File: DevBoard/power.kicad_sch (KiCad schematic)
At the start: 31 parts, among them U201 INA190A5IDDFR, U202 INA190A1IDDFR, U203 HT7550-1, U204 TPS62177DQCR

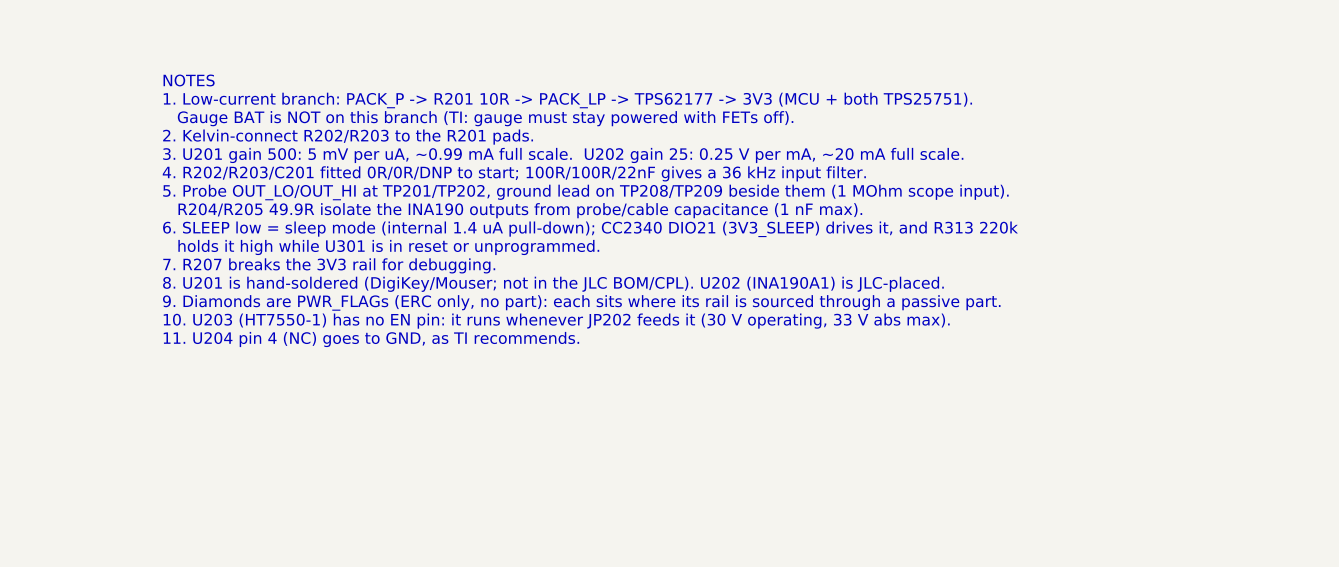
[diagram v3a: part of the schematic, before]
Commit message: Dev board: cut JLC extended parts 37 -> 27 for a 2-board build
tools/bom_fee_cut.py (one-shot); README item 44. At 2 boards the costed
BOM goes from $124.28 to $108.49 per board.
- Basic/preferred swaps, no footprint changes: C313 -> C1548, C315/C314
  -> C1550, C401/C402 -> C1530 (X7R), R433/R434 -> 120k/22k 1 %
  (PP5V 5.16 V), C443/C543 -> 100 uF 35 V Honor polymer (same as C421).
- Hand-fit from LCSC: BT101-BT104, the 13 Harwin test loops, U202, D105
  (dev-only; out of the position file).
- Board: fields refreshed by netlist_to_board.py; also includes Logan's
  block move made in KiCad. DRC parity 0; ERC unchanged.

Co-Authored-By: Claude Opus 5.5 <noreply@anthropic.com>
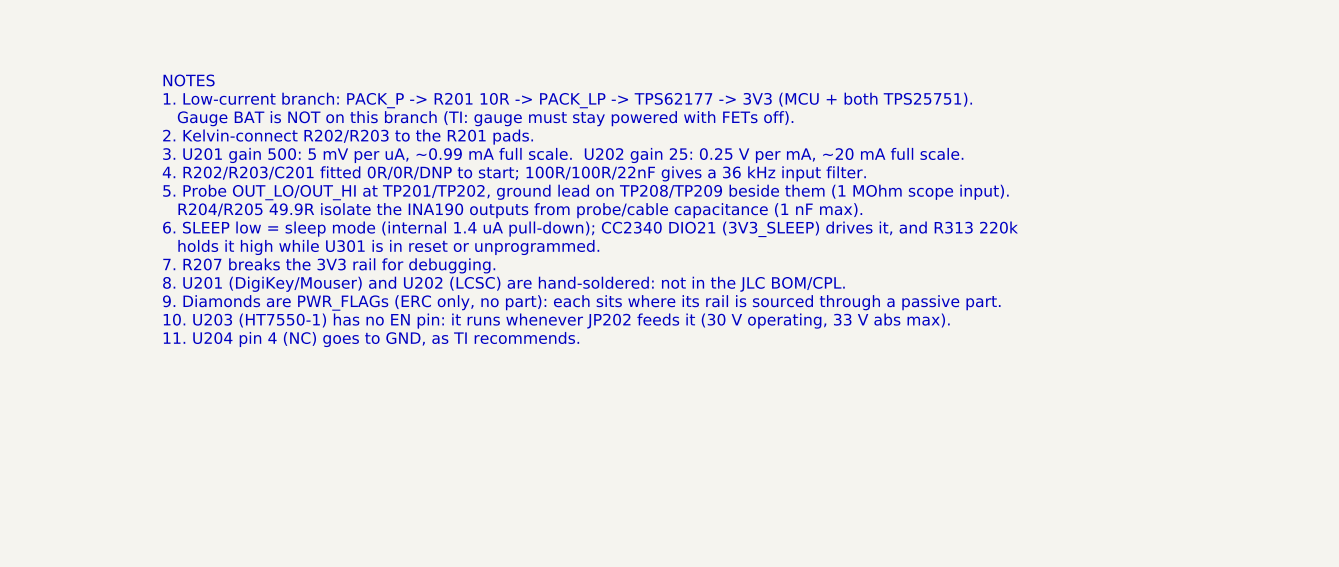
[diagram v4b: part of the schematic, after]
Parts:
- TP201, TP202, TP203, TP208, TP209: LCSC C55121754 -> (none); Sourcing (none) -> Hand-solder, not JLC assembled (test loop, dev only; saves 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
- U202: LCSC C1852068 -> (none); Sourcing JLC assembled (LCSC C1852068, 1,700 in stock 2026-10-13) -> Hand-solder, not JLC assembled (dev-only sleep-current ampl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
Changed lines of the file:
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@@
 		)
 	)
-	(text "NOTES\n1. Low-current branch: PACK_P -> R201 10R -> PACK_LP -> TPS62177 -> 3V3 (MCU + both TPS25751).\n   Gauge BAT is NOT on this branch (TI: gauge must stay powered with FETs off).\n2. Kelvin-connect R202/R203 to the R201 pads.\n3. U201 gain 500: 5 mV per uA, ~0.99 mA full scale.  U202 gain 25: 0.25 V per mA, ~20 mA full scale.\n4. R202/R203/C201 fitted 0R/0R/DNP to start; 100R/100R/22nF gives a 36 kHz input filter.\n5. Probe OUT_LO/OUT_HI at TP201/TP202, ground lead on TP208/TP209 beside them (1 MOhm scope input).\n   R204/R205 49.9R isolate the INA190 outputs from probe/cable capacitance (1 nF max).\n6. SLEEP low = sleep mode (internal 1.4 uA pull-down); CC2340 DIO21 (3V3_SLEEP) drives it, and R313 220k\n   holds it high while U301 is in reset or unprogrammed.\n7. R207 breaks the 3V3 rail for debugging.\n8. U201 is hand-soldered (DigiKey/Mouser; not in the JLC BOM/CPL). U202 (INA190A1) is JLC-placed.\n9. Diamonds are PWR_FLAGs (ERC only, no part): each sits where its rail is sourced through a passive part.\n10. U203 (HT7550-1) has no EN pin: it runs whenever JP202 feeds it (30 V operating, 33 V abs max).\n11. U204 pin 4 (NC) goes to GND, as TI recommends."
+	(text "NOTES\n1. Low-current branch: PACK_P -> R201 10R -> PACK_LP -> TPS62177 -> 3V3 (MCU + both TPS25751).\n   Gauge BAT is NOT on this branch (TI: gauge must stay powered with FETs off).\n2. Kelvin-connect R202/R203 to the R201 pads.\n3. U201 gain 500: 5 mV per uA, ~0.99 mA full scale.  U202 gain 25: 0.25 V per mA, ~20 mA full scale.\n4. R202/R203/C201 fitted 0R/0R/DNP to start; 100R/100R/22nF gives a 36 kHz input filter.\n5. Probe OUT_LO/OUT_HI at TP201/TP202, ground lead on TP208/TP209 beside them (1 MOhm scope input).\n   R204/R205 49.9R isolate the INA190 outputs from probe/cable capacitance (1 nF max).\n6. SLEEP low = sleep mode (internal 1.4 uA pull-down); CC2340 DIO21 (3V3_SLEEP) drives it, and R313 220k\n   holds it high while U301 is in reset or unprogrammed.\n7. R207 breaks the 3V3 rail for debugging.\n8. U201 (DigiKey/Mouser) and U202 (LCSC) are hand-soldered: not in the JLC BOM/CPL.\n9. Diamonds are PWR_FLAGs (ERC only, no part): each sits where its rail is sourced through a passive part.\n10. U203 (HT7550-1) has no EN pin: it runs whenever JP202 feeds it (30 V operating, 33 V abs max).\n11. U204 pin 4 (NC) goes to GND, as TI recommends."
 		(exclude_from_sim no)
 		(at 215.9 129.54 0)
@@
 		(in_bom yes)
 		(on_board yes)
-		(in_pos_files yes)
+		(in_pos_files no)
 		(dnp no)
 		(property "Reference" "TP203"
@@
 			)
 		)
-		(property "LCSC" "C55121754"
+		(property "LCSC" ""
 			(at 190.5 165.1 0)
 			(hide yes)
@@
 			)
 		)
+		(property "Sourcing" "Hand-solder, not JLC assembled (test loop, dev only; saves a JLC extended-part fee; LCSC C55121754 RH-S2761-46R (ronghe; Harwin S2761-46R equivalent))"
+			(at 190.5 165.1 0)
+			(hide yes)
+			(show_name no)
+			(do_not_autoplace no)
+			(effects
+				(font
+					(size 1.27 1.27)
+				)
+			)
+		)
 		(pin "1"
 		)
@@
 		(in_bom yes)
 		(on_board yes)
-		(in_pos_files yes)
+		(in_pos_files no)
 		(dnp no)
 		(property "Reference" "TP201"
@@
 			)
 		)
-		(property "LCSC" "C55121754"
+		(property "LCSC" ""
 			(at 152.4 144.78 0)
 			(hide yes)
@@
 			)
 		)
+		(property "Sourcing" "Hand-solder, not JLC assembled (test loop, dev only; saves a JLC extended-part fee; LCSC C55121754 RH-S2761-46R (ronghe; Harwin S2761-46R equivalent))"
+			(at 152.4 144.78 0)
+			(hide yes)
+			(show_name no)
+			(do_not_autoplace no)
+			(effects
+				(font
+					(size 1.27 1.27)
+				)
+			)
+		)
 		(pin "1"
 		)
@@
 		(in_bom yes)
 		(on_board yes)
-		(in_pos_files yes)
+		(in_pos_files no)
 		(dnp no)
 		(property "Reference" "TP208"
@@
 			)
 		)
-		(property "LCSC" "C55121754"
+		(property "LCSC" ""
 			(at 172.72 152.4 0)
 			(hide yes)
@@
 			)
 		)
+		(property "Sourcing" "Hand-solder, not JLC assembled (test loop, dev only; saves a JLC extended-part fee; LCSC C55121754 RH-S2761-46R (ronghe; Harwin S2761-46R equivalent))"
+			(at 172.72 152.4 0)
+			(hide yes)
+			(show_name no)
+			(do_not_autoplace no)
+			(effects
+				(font
+					(size 1.27 1.27)
+				)
+			)
+		)
 		(pin "1"
 		)
@@
 		(in_bom yes)
 		(on_board yes)
-		(in_pos_files yes)
+		(in_pos_files no)
 		(dnp no)
 		(property "Reference" "TP209"
@@
 			)
 		)
-		(property "LCSC" "C55121754"
+		(property "LCSC" ""
 			(at 172.72 190.5 0)
 			(hide yes)
@@
 			)
 		)
+		(property "Sourcing" "Hand-solder, not JLC assembled (test loop, dev only; saves a JLC extended-part fee; LCSC C55121754 RH-S2761-46R (ronghe; Harwin S2761-46R equivalent))"
+			(at 172.72 190.5 0)
+			(hide yes)
+			(show_name no)
+			(do_not_autoplace no)
+			(effects
+				(font
+					(size 1.27 1.27)
+				)
+			)
+		)
 		(pin "1"
 		)
@@
 		(in_bom yes)
 		(on_board yes)
-		(in_pos_files yes)
+		(in_pos_files no)
 		(dnp no)
 		(property "Reference" "U202"
@@
 			)
 		)
-		(property "LCSC" "C1852068"
+		(property "LCSC" ""
 			(at 109.22 182.88 0)
 			(hide yes)
@@
 			)
 		)
-		(property "Sourcing" "JLC assembled (LCSC C1852068, 1,700 in stock 2026-10-13)"
+		(property "Sourcing" "Hand-solder, not JLC assembled (dev-only sleep-current amplifier; saves a JLC extended-part fee; LCSC C1852068 TI INA190A1IDDFR)"
 			(at 109.22 182.88 0)
 			(hide yes)
@@
 		(in_bom yes)
 		(on_board yes)
-		(in_pos_files yes)
+		(in_pos_files no)
 		(dnp no)
 		(property "Reference" "TP202"
@@
 			)
 		)
-		(property "LCSC" "C55121754"
+		(property "LCSC" ""
 			(at 152.4 182.88 0)
 			(hide yes)
@@
 			(at 152.4 182.88 0)
 			(hide yes)
+			(show_name no)
+			(do_not_autoplace no)
+			(effects
+				(font
+					(size 1.27 1.27)
+				)
+			)
+		)
+		(property "Sourcing" "Hand-solder, not JLC assembled (test loop, dev only; saves a JLC extended-part fee; LCSC C55121754 RH-S2761-46R (ronghe; Harwin S2761-46R equivalent))"
+			(at 152.4 182.88 0)
+			(hide yes)

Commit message: Dev board: downsize passives to 0402 where basic parts allow
160 resistors and capacitors move to the smallest package that keeps their
rating: never below 0402, and no JLC basic part becomes extended. Connectivity
and ERC are unchanged, extended parts stay at 27, and the cost goes from
$108.49 to $107.93 per board at 2 boards. Applied by
tools/downsize_passives.py (one-shot); README item 45 lists what moved, what
stayed and why. The PCB still needs Update PCB from Schematic.

Co-Authored-By: Claude Opus 5.5 <noreply@anthropic.com>
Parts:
- C202, C203: footprint Capacitor_SMD:C_0603_1608Metric -> Capacitor_SMD:C_0402_1005Metric; LCSC C14663 -> C307331; MPN CC0603KRX7R9BB104 -> CL05B104KB54PNC
- C204: footprint Capacitor_SMD:C_1206_3216Metric -> Capacitor_SMD:C_0805_2012Metric; LCSC C13585 -> C440198; MPN CL31A106KBHNNNE -> GRM21BR61H106KE43L
- C205: footprint Capacitor_SMD:C_0805_2012Metric -> Capacitor_SMD:C_0603_1608Metric; LCSC C15850 -> C96446; MPN CL21A106KAYNNNE -> CL10A106MA8NRNC
- C206: footprint Capacitor_SMD:C_1206_3216Metric -> Capacitor_SMD:C_0805_2012Metric; LCSC C50254 -> C377773; MPN CL31B225KBHNNNE -> CL21A225KBQNNNE
- R202, R203: footprint Resistor_SMD:R_0603_1608Metric -> Resistor_SMD:R_0402_1005Metric; LCSC C21189 -> C17168; MPN 0603WAF0000T5E -> 0402WGF0000TCE
- R204, R205: footprint Resistor_SMD:R_0603_1608Metric -> Resistor_SMD:R_0402_1005Metric; LCSC C23185 -> C25120; MPN 0603WAF499JT5E -> 0402WGF499JTCE
- R206, R208: footprint Resistor_SMD:R_0603_1608Metric -> Resistor_SMD:R_0402_1005Metric; LCSC C25803 -> C25741; MPN 0603WAF1003T5E -> 0402WGF1003TCE
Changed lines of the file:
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@@
 			)
 		)
-		(property "Footprint" "Capacitor_SMD:C_1206_3216Metric"
+		(property "Footprint" "Capacitor_SMD:C_0805_2012Metric"
 			(at 69.545 229.87 0)
 			(hide yes)
@@
 			)
 		)
-		(property "LCSC" "C13585"
+		(property "LCSC" "C440198"
 			(at 68.58 233.68 0)
 			(hide yes)
@@
 			)
 		)
-		(property "MPN" "CL31A106KBHNNNE"
+		(property "MPN" "GRM21BR61H106KE43L"
 			(at 68.58 233.68 0)
 			(hide yes)
@@
 			)
 		)
-		(property "Footprint" "Capacitor_SMD:C_0805_2012Metric"
+		(property "Footprint" "Capacitor_SMD:C_0603_1608Metric"
 			(at 107.645 229.87 0)
 			(hide yes)
@@
 			)
 		)
-		(property "LCSC" "C15850"
+		(property "LCSC" "C96446"
 			(at 106.68 233.68 0)
 			(hide yes)
@@
 			)
 		)
-		(property "MPN" "CL21A106KAYNNNE"
+		(property "MPN" "CL10A106MA8NRNC"
 			(at 106.68 233.68 0)
 			(hide yes)
@@
 			)
 		)
-		(property "Footprint" "Resistor_SMD:R_0603_1608Metric"
+		(property "Footprint" "Resistor_SMD:R_0402_1005Metric"
 			(at 66.04 141.478 90)
 			(hide yes)
@@
 			)
 		)
-		(property "LCSC" "C21189"
+		(property "LCSC" "C17168"
 			(at 66.04 139.7 0)
 			(hide yes)
@@
 			)
 		)
-		(property "MPN" "0603WAF0000T5E"
+		(property "MPN" "0402WGF0000TCE"
 			(at 66.04 139.7 0)
 			(hide yes)
@@
 			)
 		)
-		(property "Footprint" "Capacitor_SMD:C_1206_3216Metric"
+		(property "Footprint" "Capacitor_SMD:C_0805_2012Metric"
 			(at 122.885 59.69 0)
 			(hide yes)
@@
 			)
 		)
-		(property "LCSC" "C50254"
+		(property "LCSC" "C377773"
 			(at 121.92 63.5 0)
 			(hide yes)
@@
 			)
 		)
-		(property "MPN" "CL31B225KBHNNNE"
+		(property "MPN" "CL21A225KBQNNNE"
 			(at 121.92 63.5 0)
 			(hide yes)
@@
 			)
 		)
-		(property "Footprint" "Resistor_SMD:R_0603_1608Metric"
+		(property "Footprint" "Resistor_SMD:R_0402_1005Metric"
 			(at 66.04 156.718 90)
 			(hide yes)
@@
 			)
 		)
-		(property "LCSC" "C21189"
+		(property "LCSC" "C17168"
 			(at 66.04 154.94 0)
 			(hide yes)
@@
 			)
 		)
-		(property "MPN" "0603WAF0000T5E"
+		(property "MPN" "0402WGF0000TCE"
 			(at 66.04 154.94 0)
 			(hide yes)
@@
 			)
 		)
-		(property "Footprint" "Resistor_SMD:R_0603_1608Metric"
+		(property "Footprint" "Resistor_SMD:R_0402_1005Metric"
 			(at 140.462 233.68 90)
 			(hide yes)
@@
 			)
 		)
-		(property "LCSC" "C25803"
+		(property "LCSC" "C25741"
 			(at 142.24 233.68 0)
 			(hide yes)
@@
 			)
 		)
-		(property "MPN" "0603WAF1003T5E"
+		(property "MPN" "0402WGF1003TCE"
 			(at 142.24 233.68 0)
 			(hide yes)
@@
 			)
 		)
-		(property "Footprint" "Resistor_SMD:R_0603_1608Metric"
+		(property "Footprint" "Resistor_SMD:R_0402_1005Metric"
 			(at 139.7 146.558 90)
 			(hide yes)
@@
 			)
 		)
-		(property "LCSC" "C23185"
+		(property "LCSC" "C25120"
 			(at 139.7 144.78 0)
 			(hide yes)
@@
 			)
 		)
-		(property "MPN" "0603WAF499JT5E"
+		(property "MPN" "0402WGF499JTCE"
 			(at 139.7 144.78 0)
 			(hide yes)
@@
 			)
 		)
-		(property "Footprint" "Resistor_SMD:R_0603_1608Metric"
+		(property "Footprint" "Resistor_SMD:R_0402_1005Metric"
 			(at 139.7 184.658 90)
 			(hide yes)
@@
 			)
 		)
-		(property "LCSC" "C23185"
+		(property "LCSC" "C25120"
 			(at 139.7 182.88 0)
 			(hide yes)
@@
 			)
 		)
-		(property "MPN" "0603WAF499JT5E"
+		(property "MPN" "0402WGF499JTCE"
 			(at 139.7 182.88 0)
 			(hide yes)
@@
 			)
 		)
-		(property "Footprint" "Capacitor_SMD:C_0603_1608Metric"
+		(property "Footprint" "Capacitor_SMD:C_0402_1005Metric"
 			(at 130.505 170.18 0)
 			(hide yes)
@@
 			)
 		)
-		(property "LCSC" "C14663"
+		(property "LCSC" "C307331"
 			(at 129.54 173.99 0)
 			(hide yes)
@@
 			)
 		)
-		(property "MPN" "CC0603KRX7R9BB104"
+		(property "MPN" "CL05B104KB54PNC"
 			(at 129.54 173.99 0)
 			(hide yes)
@@
 			)
 		)
-		(property "Footprint" "Capacitor_SMD:C_0603_1608Metric"
+		(property "Footprint" "Capacitor_SMD:C_0402_1005Metric"
 			(at 130.505 132.08 0)
 			(hide yes)
@@
 			)
 		)
-		(property "LCSC" "C14663"
+		(property "LCSC" "C307331"
 			(at 129.54 135.89 0)
 			(hide yes)
@@
 			)
 		)
-		(property "MPN" "CC0603KRX7R9BB104"
+		(property "MPN" "CL05B104KB54PNC"
 			(at 129.54 135.89 0)
 			(hide yes)
@@
 			)
 		)
-		(property "Footprint" "Resistor_SMD:R_0603_1608Metric"
+		(property "Footprint" "Resistor_SMD:R_0402_1005Metric"
 			(at 132.842 72.39 90)
 			(hide yes)
@@
 			)
 		)
-		(property "LCSC" "C25803"
+		(property "LCSC" "C25741"
 			(at 134.62 72.39 0)
 			(hide yes)
@@
 			)
 		)
-		(property "MPN" "0603WAF1003T5E"
+		(property "MPN" "0402WGF1003TCE"
 			(at 134.62 72.39 0)
 			(hide yes)
